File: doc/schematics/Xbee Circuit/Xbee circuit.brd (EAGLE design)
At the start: 100 x 80 mm, 11 parts

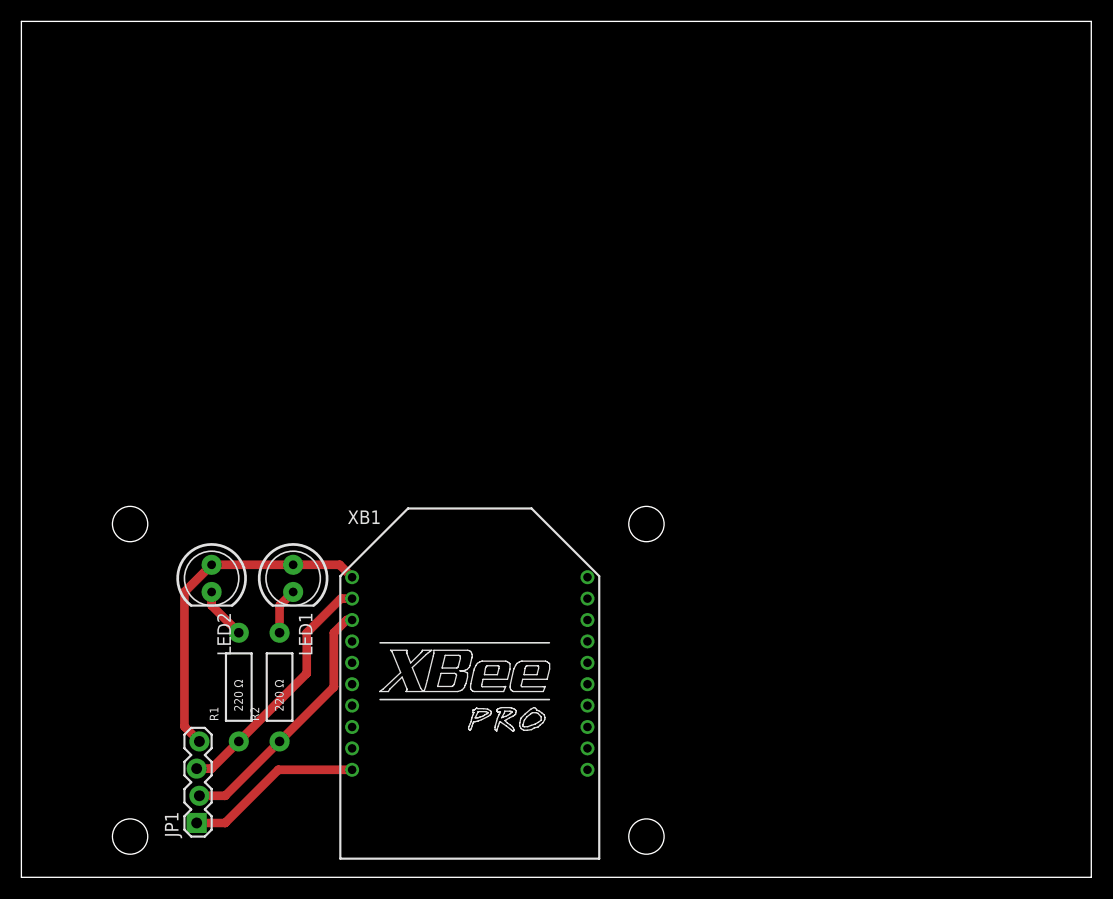
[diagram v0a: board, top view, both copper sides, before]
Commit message: Started the barometer message, hit a strange error.
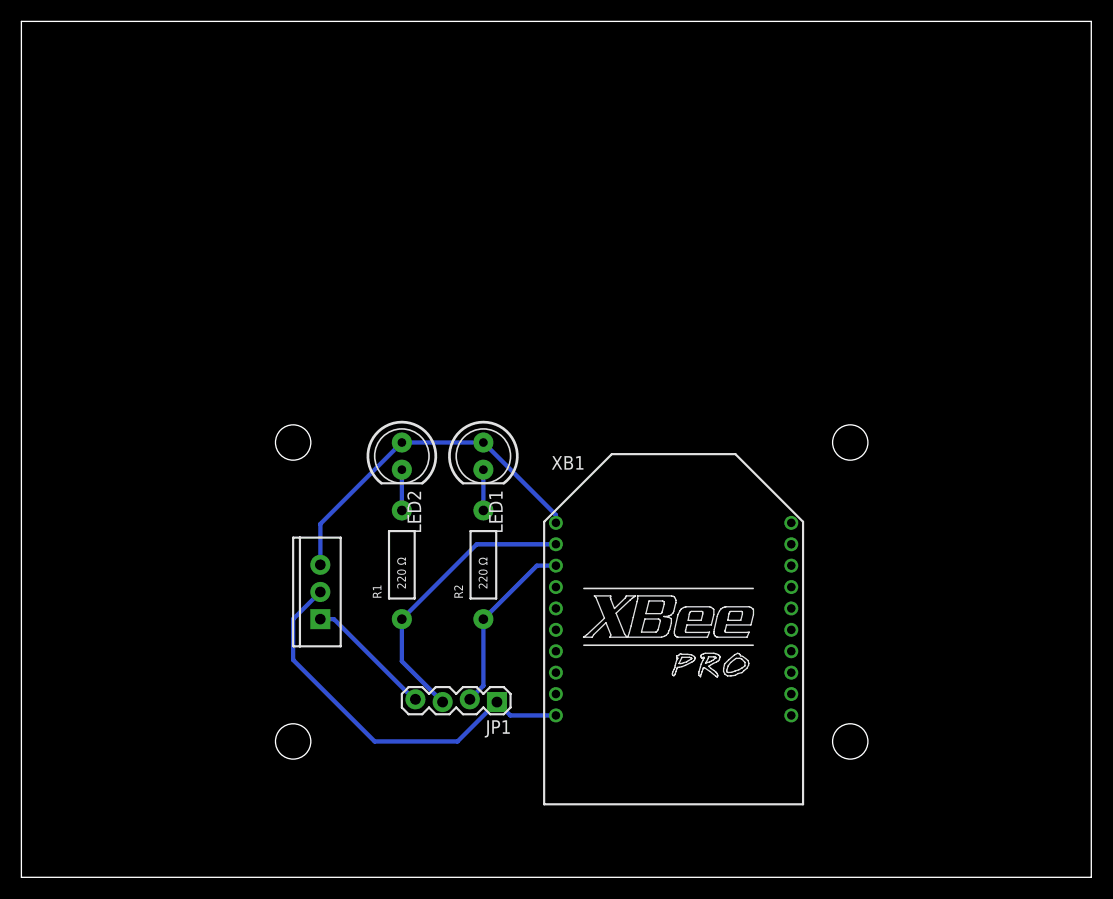
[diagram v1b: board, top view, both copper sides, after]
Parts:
- added IC1: (no value), SparkFun-PowerIC:TO220-IGO
- moved JP1 30.2 mm to (44.5, 16.5), turned to 180 degrees
- moved R2 22.2 mm to (43.2, 29.2)
- moved LED1 21.1 mm to (43.2, 39.4)
- moved LED2 21.1 mm to (35.6, 39.4)
- moved U$3 21.0 mm to (77.5, 12.7)
- moved U$4 20.5 mm to (77.5, 40.6)
- moved XB1 19.7 mm to (61.0, 24.1)
- moved R1 19.1 mm to (35.6, 29.2)
- moved U$2 17.6 mm to (25.4, 12.7)
- moved U$1 17.0 mm to (25.4, 40.6)
- moved FRAME1 11.7 mm to (33.0, -6.35)
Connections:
- new net N$5: IC1.IN, JP1.4
- net GND: now also IC1.GND
- net VCC: now also IC1.OUT; no longer JP1.4
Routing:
- net GND: track 16.5 -> 37.2 mm
- net N$5: track 0.00 -> 12.2 mm
- net N$3: track 24.1 -> 16.9 mm
- net N$4: track 23.3 -> 26.6 mm
- net N$1: track 4.86 -> 3.81 mm
- net VCC: track 31.8 -> 32.5 mm
- net N$2: track 4.34 -> 3.81 mm
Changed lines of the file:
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@@
 <layer number="106" name="bPlate" color="7" fill="1" visible="no" active="yes"/>
 <layer number="107" name="Crop" color="7" fill="1" visible="no" active="yes"/>
+<layer number="108" name="tplace-old" color="10" fill="1" visible="yes" active="yes"/>
+<layer number="109" name="ref-old" color="11" fill="1" visible="yes" active="yes"/>
 <layer number="116" name="Patch_BOT" color="9" fill="4" visible="no" active="yes"/>
 <layer number="121" name="_tsilk" color="7" fill="1" visible="no" active="yes"/>
@@
 </autorouter>
 <elements>
-<element name="XB1" library="maxstream" package="XBEE-PRO" value="XBEE-PRO" x="41.91" y="19.05">
-<attribute name="OC_NEWARK" value="42M2667" x="67.31" y="-1.27" size="1.778" layer="27" display="off"/>
-<attribute name="MPN" value="XBP24-AWI-001" x="67.31" y="-1.27" size="1.778" layer="27" display="off"/>
-<attribute name="MF" value="" x="67.31" y="-1.27" size="1.778" layer="27" display="off"/>
-<attribute name="OC_FARNELL" value="1337916" x="67.31" y="-1.27" size="1.778" layer="27" display="off"/>
+<element name="XB1" library="maxstream" package="XBEE-PRO" value="XBEE-PRO" x="60.96" y="24.13">
+<attribute name="OC_NEWARK" value="42M2667" x="86.36" y="3.81" size="1.778" layer="27" display="off"/>
+<attribute name="MPN" value="XBP24-AWI-001" x="86.36" y="3.81" size="1.778" layer="27" display="off"/>
+<attribute name="MF" value="" x="86.36" y="3.81" size="1.778" layer="27" display="off"/>
+<attribute name="OC_FARNELL" value="1337916" x="86.36" y="3.81" size="1.778" layer="27" display="off"/>
 </element>
-<element name="LED1" library="SparkFun-LED" package="LED5MM" value="" x="25.4" y="27.94" rot="R270"/>
-<element name="LED2" library="SparkFun-LED" package="LED5MM" value="" x="17.78" y="27.94" rot="R270"/>
-<element name="R1" library="SparkFun-Resistors" package="AXIAL-0.4" value="220 Ω" x="20.32" y="17.78" rot="R90"/>
-<element name="R2" library="SparkFun-Resistors" package="AXIAL-0.4" value="220 Ω" x="24.13" y="17.78" rot="R90"/>
-<element name="JP1" library="SparkFun-Connectors" package="1X04_LOCK" value="" x="16.51" y="5.08" rot="R90"/>
-<element name="U$1" library="SparkFun-Electromechanical" package="STAND-OFF" value="" x="10.16" y="33.02"/>
-<element name="FRAME1" library="SparkFun-Aesthetics" package="CREATIVE_COMMONS" value="FRAME-LETTER" x="21.59" y="-8.89"/>
-<element name="U$2" library="SparkFun-Electromechanical" package="STAND-OFF" value="" x="10.16" y="3.81"/>
-<element name="U$3" library="SparkFun-Electromechanical" package="STAND-OFF" value="" x="58.42" y="3.81"/>
-<element name="U$4" library="SparkFun-Electromechanical" package="STAND-OFF" value="" x="58.42" y="33.02"/>
+<element name="LED1" library="SparkFun-LED" package="LED5MM" value="" x="43.18" y="39.37" rot="R270"/>
+<element name="LED2" library="SparkFun-LED" package="LED5MM" value="" x="35.56" y="39.37" rot="R270"/>
+<element name="R1" library="SparkFun-Resistors" package="AXIAL-0.4" value="220 Ω" x="35.56" y="29.21" rot="R90"/>
+<element name="R2" library="SparkFun-Resistors" package="AXIAL-0.4" value="220 Ω" x="43.18" y="29.21" rot="R90"/>
+<element name="JP1" library="SparkFun-Connectors" package="1X04_LOCK" value="" x="44.45" y="16.51" rot="R180"/>
+<element name="U$1" library="SparkFun-Electromechanical" package="STAND-OFF" value="" x="25.4" y="40.64"/>
+<element name="FRAME1" library="SparkFun-Aesthetics" package="CREATIVE_COMMONS" value="FRAME-LETTER" x="33.02" y="-6.35"/>
+<element name="U$2" library="SparkFun-Electromechanical" package="STAND-OFF" value="" x="25.4" y="12.7"/>
+<element name="U$3" library="SparkFun-Electromechanical" package="STAND-OFF" value="" x="77.47" y="12.7"/>
+<element name="U$4" library="SparkFun-Electromechanical" package="STAND-OFF" value="" x="77.47" y="40.64"/>
+<element name="IC1" library="SparkFun-PowerIC" package="TO220-IGO" value="" x="27.94" y="26.67" rot="R90"/>
 </elements>
 <signals>
@@
 <contactref element="LED2" pad="A"/>
 <contactref element="LED1" pad="A"/>
-<contactref element="JP1" pad="4"/>
-<wire x1="30.91" y1="28.05" x2="29.75" y2="29.21" width="0.8128" layer="1"/>
-<wire x1="29.75" y1="29.21" x2="25.4" y2="29.21" width="0.8128" layer="1"/>
-<wire x1="25.4" y1="29.21" x2="17.78" y2="29.21" width="0.8128" layer="1"/>
-<wire x1="17.78" y1="29.21" x2="15.24" y2="26.67" width="0.8128" layer="1"/>
-<wire x1="15.24" y1="26.67" x2="15.24" y2="14.097" width="0.8128" layer="1"/>
-<wire x1="15.24" y1="14.097" x2="16.637" y2="12.7" width="0.8128" layer="1"/>
+<contactref element="IC1" pad="OUT"/>
+<wire x1="49.96" y1="33.13" x2="49.96" y2="33.86" width="0.4064" layer="16"/>
+<wire x1="49.96" y1="33.86" x2="43.18" y2="40.64" width="0.4064" layer="16"/>
+<wire x1="43.18" y1="40.64" x2="35.56" y2="40.64" width="0.4064" layer="16"/>
+<wire x1="35.56" y1="40.64" x2="27.94" y2="33.02" width="0.4064" layer="16"/>
+<wire x1="27.94" y1="33.02" x2="27.94" y2="29.21" width="0.4064" layer="16"/>
 </signal>
 <signal name="GND">
 <contactref element="XB1" pad="10"/>
+<contactref element="IC1" pad="GND"/>
 <contactref element="JP1" pad="1"/>
-<wire x1="30.91" y1="10.05" x2="24.02" y2="10.05" width="0.8128" layer="1"/>
-<wire x1="24.02" y1="10.05" x2="19.05" y2="5.08" width="0.8128" layer="1"/>
-<wire x1="19.05" y1="5.08" x2="16.51" y2="5.08" width="0.8128" layer="1"/>
-<wire x1="16.51" y1="5.08" x2="16.383" y2="5.08" width="0" layer="19" extent="1-16"/>
+<wire x1="49.96" y1="15.13" x2="45.703" y2="15.13" width="0.4064" layer="16"/>
+<wire x1="45.703" y1="15.13" x2="44.45" y2="16.383" width="0.4064" layer="16"/>
+<wire x1="27.94" y1="26.67" x2="25.4" y2="24.13" width="0.4064" layer="16"/>
+<wire x1="25.4" y1="24.13" x2="25.4" y2="20.32" width="0.4064" layer="16"/>
+<wire x1="25.4" y1="20.32" x2="33.02" y2="12.7" width="0.4064" layer="16"/>
+<wire x1="33.02" y1="12.7" x2="40.767" y2="12.7" width="0.4064" layer="16"/>
+<wire x1="40.767" y1="12.7" x2="44.45" y2="16.383" width="0.4064" layer="16"/>
 </signal>
 <signal name="N$1">
 <contactref element="LED2" pad="K"/>
 <contactref element="R1" pad="P$2"/>
-<wire x1="17.78" y1="26.67" x2="17.78" y2="25.4" width="0.8128" layer="1"/>
-<wire x1="17.78" y1="25.4" x2="20.32" y2="22.86" width="0.8128" layer="1"/>
+<wire x1="35.56" y1="38.1" x2="35.56" y2="34.29" width="0.4064" layer="16"/>
 </signal>
 <signal name="N$2">
 <contactref element="LED1" pad="K"/>
 <contactref element="R2" pad="P$2"/>
-<wire x1="25.4" y1="26.67" x2="24.13" y2="25.4" width="0.8128" layer="1"/>
-<wire x1="24.13" y1="25.4" x2="24.13" y2="22.86" width="0.8128" layer="1"/>
+<wire x1="43.18" y1="38.1" x2="43.18" y2="34.29" width="0.4064" layer="16"/>
 </signal>
 <signal name="N$3">
@@
 <contactref element="R2" pad="P$1"/>
 <contactref element="JP1" pad="2"/>
-<wire x1="30.91" y1="24.05" x2="30.4" y2="24.05" width="0.8128" layer="1"/>
-<wire x1="30.4" y1="24.05" x2="29.21" y2="22.86" width="0.8128" layer="1"/>
-<wire x1="29.21" y1="22.86" x2="29.21" y2="17.78" width="0.8128" layer="1"/>
-<wire x1="29.21" y1="17.78" x2="24.13" y2="12.7" width="0.8128" layer="1"/>
-<wire x1="24.13" y1="12.7" x2="19.05" y2="7.62" width="0.8128" layer="1"/>
-<wire x1="19.05" y1="7.62" x2="16.637" y2="7.62" width="0.8128" layer="1"/>
+<wire x1="49.96" y1="29.13" x2="48.18" y2="29.13" width="0.4064" layer="16"/>
+<wire x1="48.18" y1="29.13" x2="43.18" y2="24.13" width="0.4064" layer="16"/>
+<wire x1="43.18" y1="24.13" x2="43.18" y2="17.907" width="0.4064" layer="16"/>
+<wire x1="43.18" y1="17.907" x2="41.91" y2="16.637" width="0.4064" layer="16"/>
 </signal>
 <signal name="N$4">
@@
 <contactref element="R1" pad="P$1"/>
 <contactref element="JP1" pad="3"/>
-<wire x1="30.91" y1="26.05" x2="29.86" y2="26.05" width="0.8128" layer="1"/>
-<wire x1="29.86" y1="26.05" x2="26.67" y2="22.86" width="0.8128" layer="1"/>
-<wire x1="26.67" y1="22.86" x2="26.67" y2="19.05" width="0.8128" layer="1"/>
-<wire x1="26.67" y1="19.05" x2="20.32" y2="12.7" width="0.8128" layer="1"/>
-<wire x1="20.32" y1="12.7" x2="17.78" y2="10.16" width="0.8128" layer="1"/>
-<wire x1="17.78" y1="10.16" x2="16.383" y2="10.16" width="0.8128" layer="1"/>
+<wire x1="49.96" y1="31.13" x2="42.56" y2="31.13" width="0.4064" layer="16"/>
+<wire x1="42.56" y1="31.13" x2="35.56" y2="24.13" width="0.4064" layer="16"/>
+<wire x1="35.56" y1="24.13" x2="35.56" y2="20.193" width="0.4064" layer="16"/>
+<wire x1="35.56" y1="20.193" x2="39.37" y2="16.383" width="0.4064" layer="16"/>
+</signal>
+<signal name="N$5">
+<contactref element="IC1" pad="IN"/>
+<contactref element="JP1" pad="4"/>
+<wire x1="27.94" y1="24.13" x2="29.21" y2="24.13" width="0.4064" layer="16"/>
+<wire x1="29.21" y1="24.13" x2="36.83" y2="16.51" width="0.4064" layer="16"/>
+<wire x1="36.83" y1="16.51" x2="36.83" y2="16.637" width="0.4064" layer="16"/>
 </signal>
 </signals>

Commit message: Schematics: XBEE finished, Compas Started Power supply: looked at.
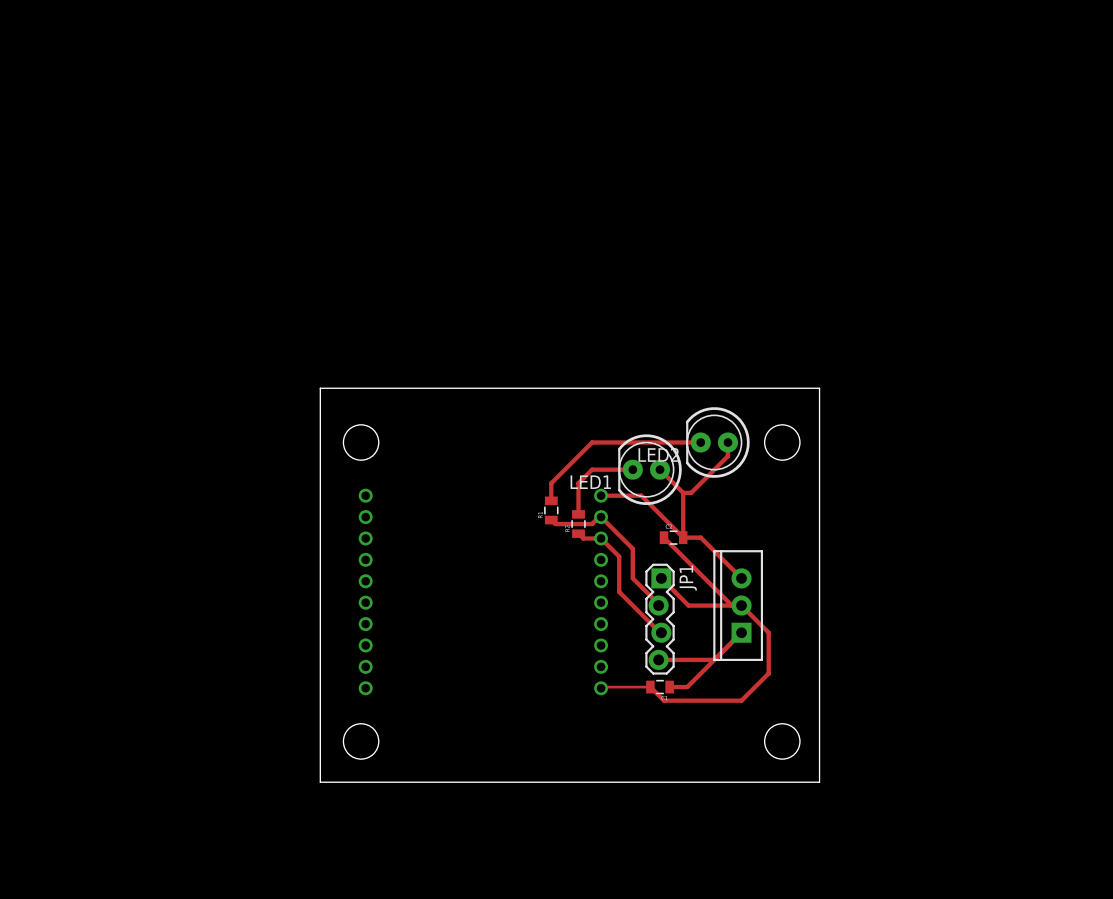
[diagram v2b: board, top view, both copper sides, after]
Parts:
- added C1: 4.7 uF, SparkFun-Capacitors:0805
- added C2: 1 uF, SparkFun-Capacitors:0805
- R1, R2: device SparkFun-Resistors:AXIAL-0.4 -> SparkFun-Resistors:0805
- moved IC1 39.4 mm to (67.3, 25.4)
- moved LED2 29.2 mm to (64.8, 40.6), turned to 180 degrees
- moved JP1 19.0 mm to (59.7, 27.9), turned to 270 degrees
- moved XB1 18.0 mm to (43.2, 26.7), flipped to the bottom
- moved LED1 15.3 mm to (58.4, 38.1), turned to 180 degrees
- moved R1 14.9 mm to (49.5, 34.3)
- moved R2 9.67 mm to (52.1, 33.0)
- moved U$1 6.35 mm to (31.8, 40.6)
- moved U$2 6.35 mm to (31.8, 12.7)
- moved U$3 6.35 mm to (71.1, 12.7)
- moved U$4 6.35 mm to (71.1, 40.6)
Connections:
- net GND: now also C1.2, C2.1
- net N$1: now also R1.2; no longer R1.P$2
- net N$2: now also R2.2; no longer R2.P$2
- net N$3: now also JP1.3, R2.1; no longer JP1.2, R2.P$1
- net N$4: now also JP1.2, R1.1; no longer JP1.3, R1.P$1
- net N$5: now also C1.1
- net VCC: now also C2.2
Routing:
- net N$1: track 3.81 -> 17.2 mm
- net N$4: track 26.6 -> 15.6 mm
- net GND: track 37.2 -> 43.1 mm
- net N$5: track 12.2 -> 17.6 mm
- net N$2: track 3.81 -> 8.52 mm
- net N$3: track 16.9 -> 13.5 mm
- net VCC: track 32.5 -> 30.5 mm
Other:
- board size 100 x 80 mm -> 46.7 x 36.8 mm
